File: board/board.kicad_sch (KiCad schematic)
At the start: 20 parts, among them J1 004_BASE-T_CT_2x3, J19 009_1000BASE-T_2x5, J20 004_BASE-T_CT_2x3, J21 009_1000BASE-T_2x5, U1 WE7490220122

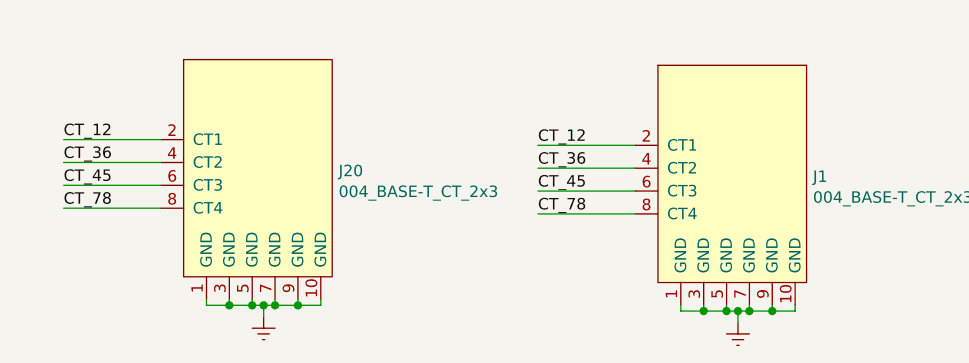
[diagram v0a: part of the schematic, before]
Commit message: refactored to use modern connectors and layout
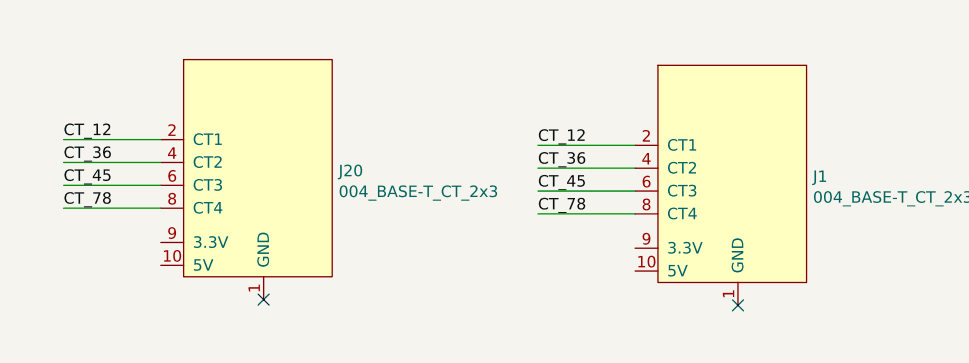
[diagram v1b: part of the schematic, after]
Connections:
- net Earth: no longer J1.1 (GND), J1.10 (GND), J1.3 (GND), J1.5 (GND), J1.7 (GND), J1.9 (GND), J20.1 (GND), J20.10 (GND), J20.3 (GND), J20.5 (GND), J20.7 (GND), J20.9 (GND)
- no-connect marks 0 -> 2
